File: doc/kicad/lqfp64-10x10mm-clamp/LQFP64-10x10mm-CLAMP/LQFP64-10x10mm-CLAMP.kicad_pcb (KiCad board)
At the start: 2 copper layers, 50 x 25 mm, 11 parts, among them J0 Conn_01x01, J1 Conn_01x16, J2 Conn_01x16, J3 Conn_01x16, J4 Conn_01x16, J5 Conn_01x12, J6 Conn_01x12, J7 Conn_01x12, J8 Conn_01x12, U1 STM32F030RCTx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

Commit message: doc/kicad: add LQFP64-10x10mm-CLAMP
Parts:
- U1: value STM32F030RCTx -> LQFP64-G
- U2: value STM32F103C8Tx -> LQFP48-G
- moved U2 1.39 mm to (76.6, 57.2)

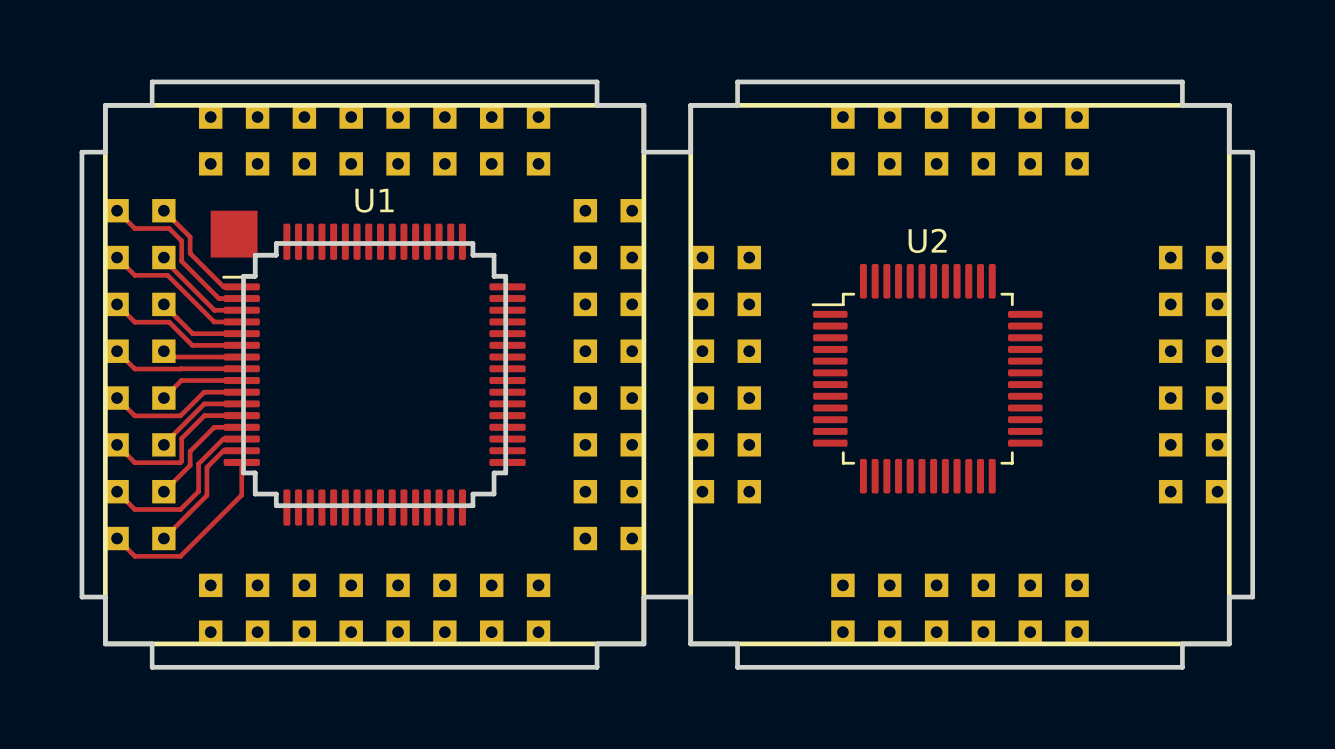
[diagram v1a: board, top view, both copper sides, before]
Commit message: doc/kicad: LQFP64-10x10mm-CLAMP PCB layout (partly)
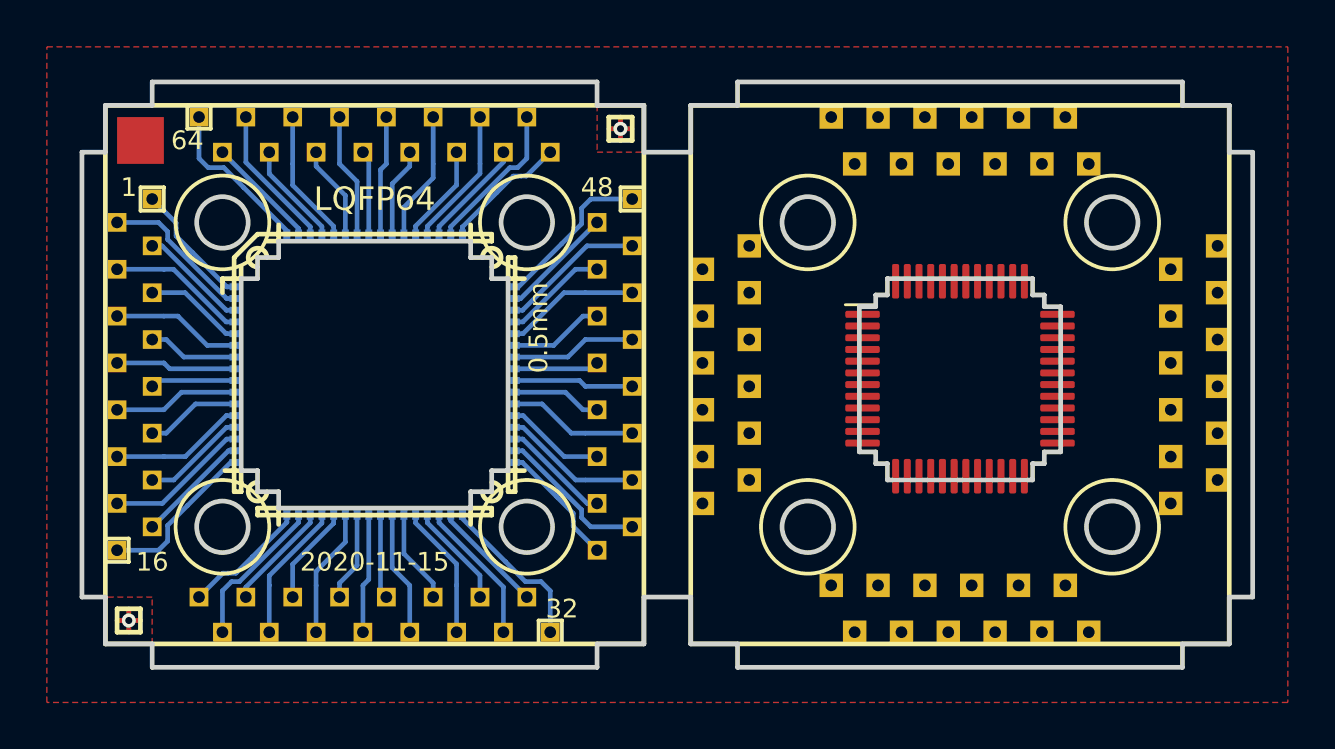
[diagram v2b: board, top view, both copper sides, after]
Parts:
- U1: footprint Package_QFP:LQFP-64_10x10mm_P0.5mm -> fmlibf:LQFP-64_10x10mm_P0.5mm_H
- U2: footprint Package_QFP:LQFP-48_7x7mm_P0.5mm -> fmlibf:LQFP-48_7x7mm_P0.5mm_H
- moved J0 5.66 mm to (43.0, 47.0)
- moved U2 1.37 mm to (78.0, 57.2)
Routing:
- net /P164: track 0.00 -> 6.87 mm
- net /P148: track 0.00 -> 6.87 mm
- net /P132: track 0.00 -> 6.87 mm
- net /P118: track 0.00 -> 6.38 mm
- net /P150: track 0.00 -> 6.38 mm
- net /P134: track 0.00 -> 6.38 mm
- net /P162: track 0.00 -> 6.08 mm
- net /P146: track 0.00 -> 6.08 mm
- net /P130: track 0.00 -> 6.08 mm
- net /P152: track 0.00 -> 5.83 mm
- net /P136: track 0.00 -> 5.83 mm
- net /P120: track 0.00 -> 5.83 mm
- net /P160: track 0.00 -> 5.62 mm
- net /P144: track 0.00 -> 5.62 mm
- net /P128: track 0.00 -> 5.62 mm
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- added copper zone on F.Cu, net GND
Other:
- outline, holes or cut-outs redrawn
- board text added: "0.5mm"
- board text added: "1"
- board text added: "16"
- board text added: "2020-11-15"
- board text added: "32"
- board text added: "48"
- board text added: "64"
- board text added: "CLAMP v0.1"
- board text added: "LQFP64"
- board text added: "P1"
